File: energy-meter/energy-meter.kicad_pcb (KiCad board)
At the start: 2 copper layers, 82 x 62.5 mm, 55 parts, among them J1 Screw_Terminal_01x04, J2 Conn_01x03, K1 G5RL-U1A-E, P1 PineNut, Q11 AP3400, T1 AP-2500, T2 BV 202 0154, U1 L9110S, U11 SLG47004, U9 GD32VF103

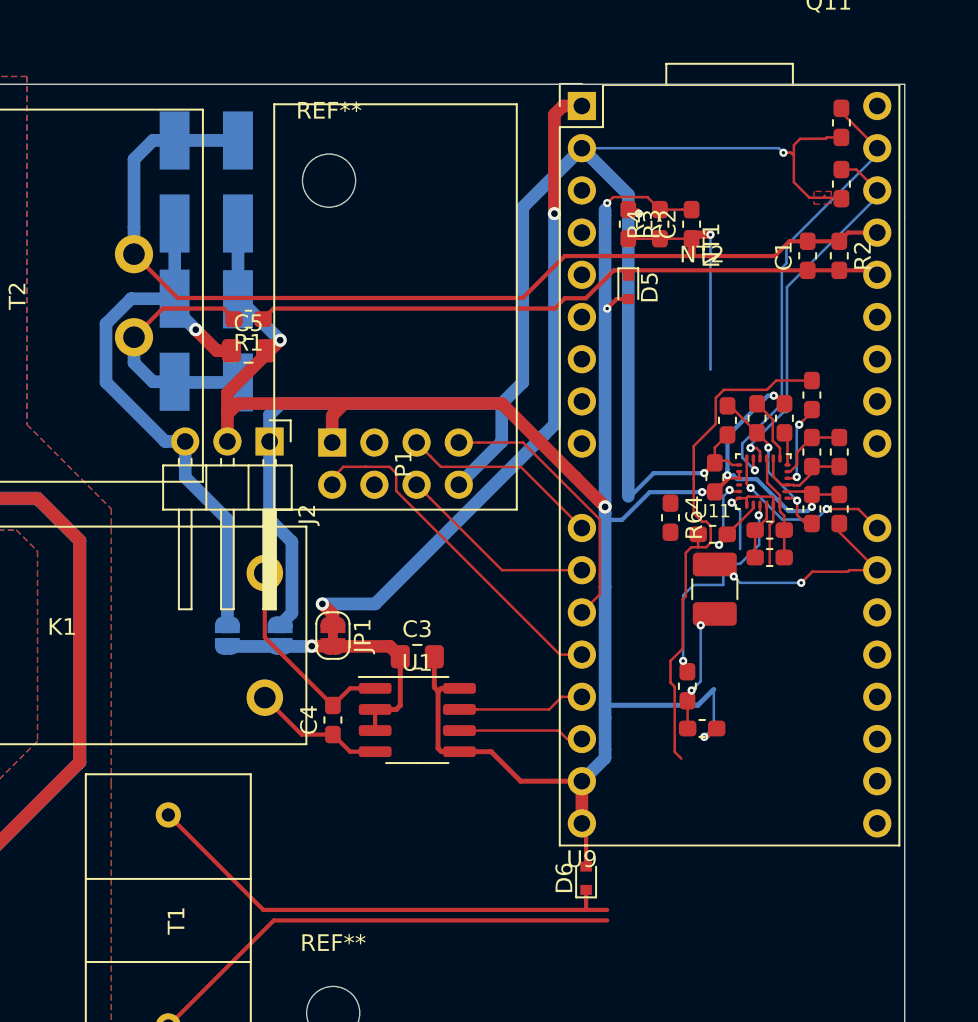
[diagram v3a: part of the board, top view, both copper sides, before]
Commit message: DRC, add header for I2C
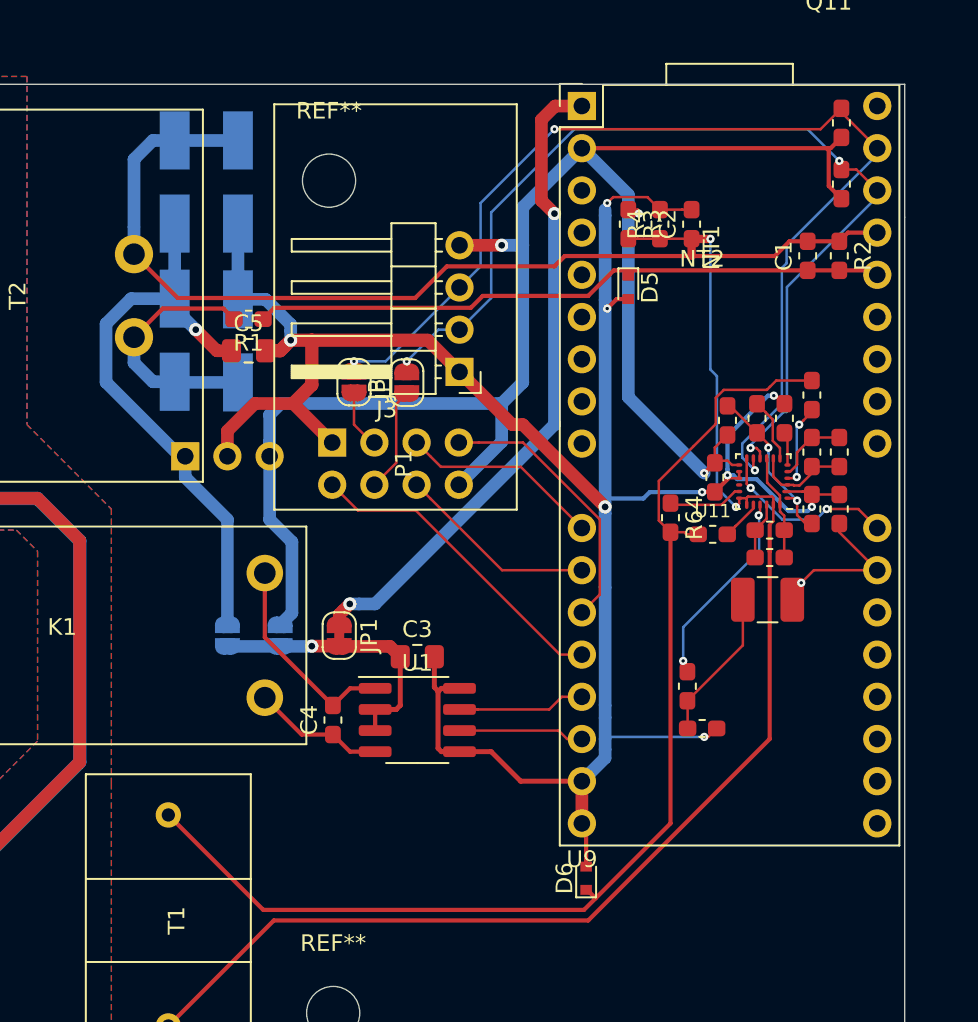
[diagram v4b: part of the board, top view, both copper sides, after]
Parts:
- added J3: I2C OLED Display, etc., Connector_PinHeader_2.54mm:PinHeader_1x04_P2.54mm_Horizontal, F.Cu at (158.3, 110.6)
- added JP4: SolderJumper_2_Open, Jumper:SolderJumper-2_P1.3mm_Open_RoundedPad1.0x1.5mm, F.Cu at (155.1, 111.3)
- added JP5: SolderJumper_2_Open, Jumper:SolderJumper-2_P1.3mm_Open_RoundedPad1.0x1.5mm, F.Cu at (151.9, 111.3)
- J2: moved to B.Cu
- moved J2 5.16 mm to (141.8, 115.7)
- moved L4 3.24 mm to (176.8, 124.4), turned to 0 degrees
- moved JP1 0.38 mm to (151.0, 126.5)
- moved NT2 0.25 mm to (172.9, 102.6)
- moved NT1 0.13 mm to (172.2, 103.2)
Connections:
- C68 pad 1: VDDA -> +3V3
- J2 pad 1: +3V3 -> +6V
- J2 pad 3: +6V -> +3V3
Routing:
- net /SDA: track 27.1 -> 65.6 mm, vias 1 -> 3
- net /SCL: track 22.5 -> 59.4 mm, vias 1 -> 3
- net /CURRENT1: track 47.3 -> 77.9 mm
- net /CURRENT0: track 61.2 -> 70.8 mm
- net Net-(JP4-Pad1): track 0.00 -> 6.30 mm
- net /OP1_OUT_F: track 14.3 -> 8.64 mm, vias 2 -> 1
- net Net-(JP5-Pad2): track 0.00 -> 3.58 mm
- net +3V3: track 106.8 -> 103.5 mm
- net /PINENUT_TX: track 21.0 -> 19.3 mm
- net Net-(C84-Pad1): track 7.79 -> 9.24 mm, vias 2 -> 0
- net /Modified LCR Meter/OP1_OUT: track 13.4 -> 12.1 mm
- net GND: track 147.2 -> 148.0 mm
- net +5V: track 40.5 -> 39.8 mm
- net +6V: track 36.2 -> 35.7 mm
- net /Modified LCR Meter/AS1A_2: track 4.77 -> 4.50 mm, vias 2 -> 0
- removed copper zone on F.Cu, net +3V3

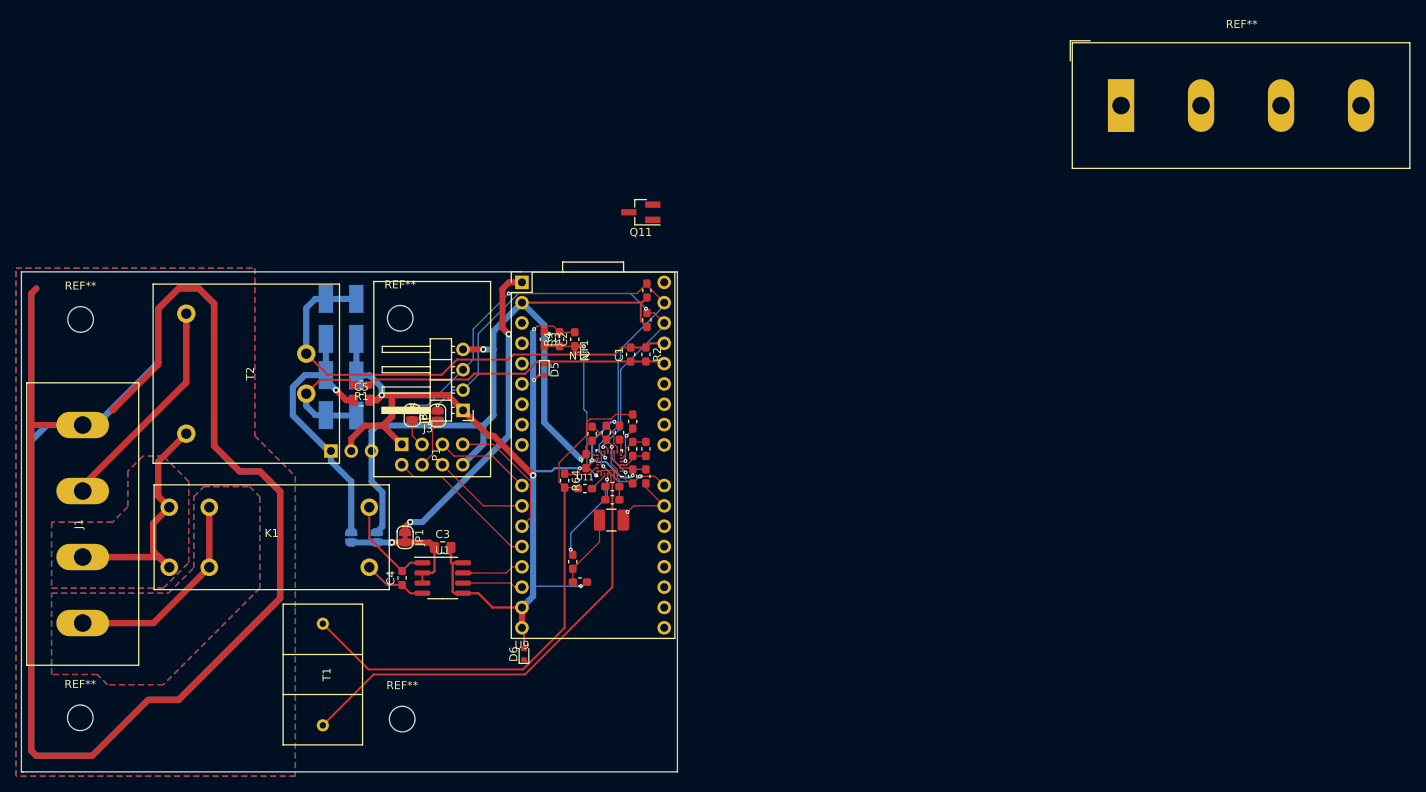
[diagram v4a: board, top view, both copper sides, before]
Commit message: add alternative relay
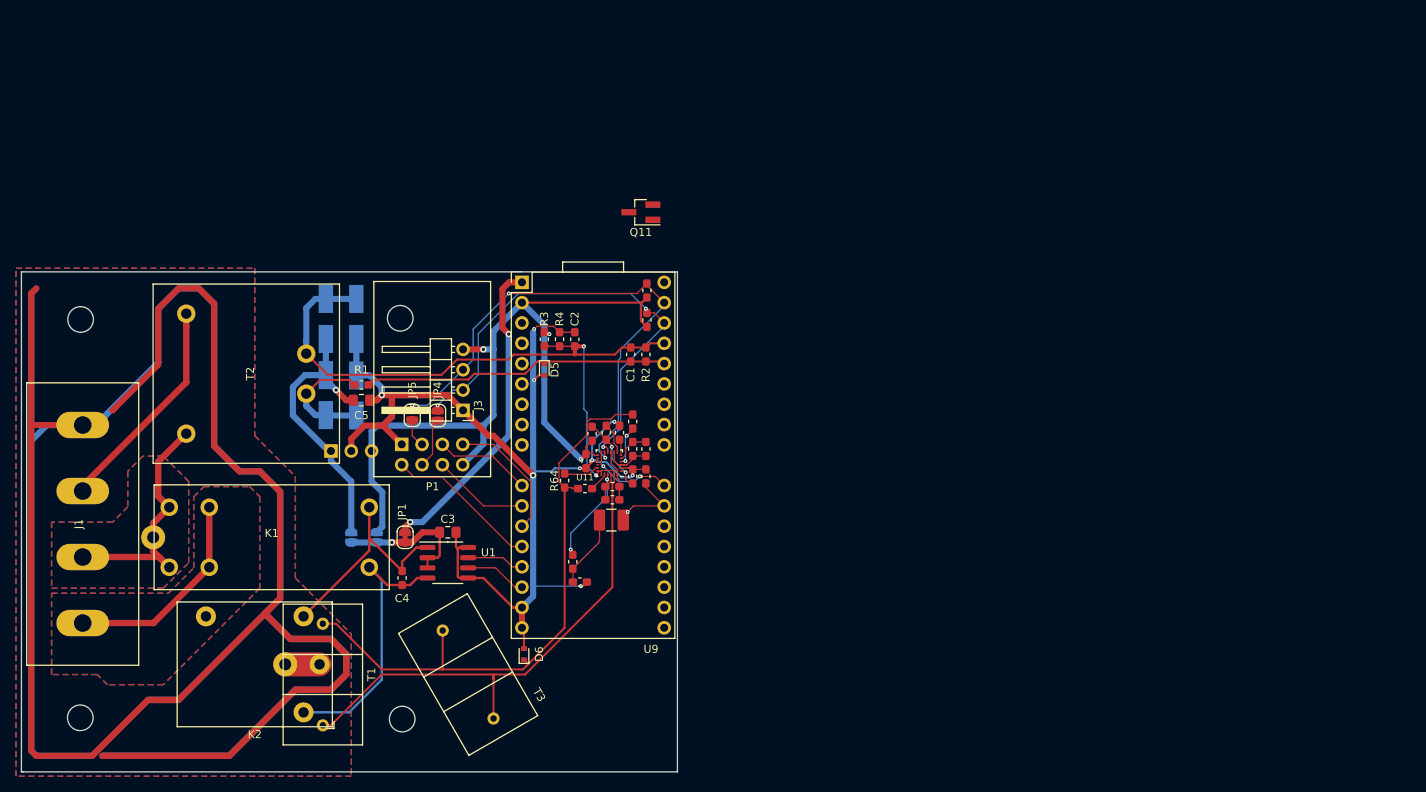
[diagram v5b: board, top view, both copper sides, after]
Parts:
- removed the REF** at (240.5, 72.5)
- added K2: DNP / HF3FF/005-1HST, energy-meter:Relay_HF3FF_005, F.Cu at (132.2, 142.4)
- added T3: DNP / AP-2500, energy-meter:AP-2500, F.Cu at (158.9, 143.7)
- added TP1: TestPoint, TestPoint:TestPoint_THTPad_D3.0mm_Drill1.5mm, B.Cu at (136.0, 142.4)
- added TP2: TestPoint, TestPoint:TestPoint_THTPad_D3.0mm_Drill1.5mm, B.Cu at (119.5, 126.5)
- moved C3 2.01 mm to (156.4, 125.9)
- moved U1 2.01 mm to (156.4, 129.7)
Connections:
- net Net-(C4-Pad1) renamed /coil-
- net Net-(C4-Pad2) renamed /coil+
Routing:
- net PE: track 344.9 -> 444.8 mm
- net /coil-: track 7.99 -> 34.7 mm
- net /coil+: track 12.6 -> 27.9 mm
- net /CURRENT1: track 77.9 -> 84.0 mm
- net /CURRENT0: track 70.8 -> 75.7 mm
- net Net-(K2-Pad1): track 0.00 -> 4.29 mm
- net Net-(C3-Pad1): track 16.5 -> 17.4 mm
